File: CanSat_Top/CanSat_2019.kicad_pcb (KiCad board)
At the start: 6 copper layers, 65 x 65 mm, 152 parts, among them J10 20 Pin FFC, J3 Conn_SWD_10, J5 505110-1292 FFC, J6 0734120114, J7 Micro_SD_Card_Det_Hirose_DM3AT, J8 AVR-ISP-6, J9 20Pin FFC, Q1 SSM3J338R, Q2 SSM3J338R, Q3 SSM3J338R, SW1 SW_Push, SW2 SW_Push, SW3 SW_Push, SW4 SW_Push, U1 INA260, U10 W25M02GV, U11 M24M02-DRMN6TB, U12 BME280, U13 BME280, U14 BME280, U15 DS18B20U, U16 DS18B20U, U17 DS18B20U, U2 STM32H743ZITx, U21 ATTINY85-20SU, U3 TPS62132, U4 PA6H, U5 RFM69HCW, U6 APDS-9960, U7 CM1624, U8 BNO055, U9 MPU-9250, Y1 SIT1533AI-H4-DCC-32_768E

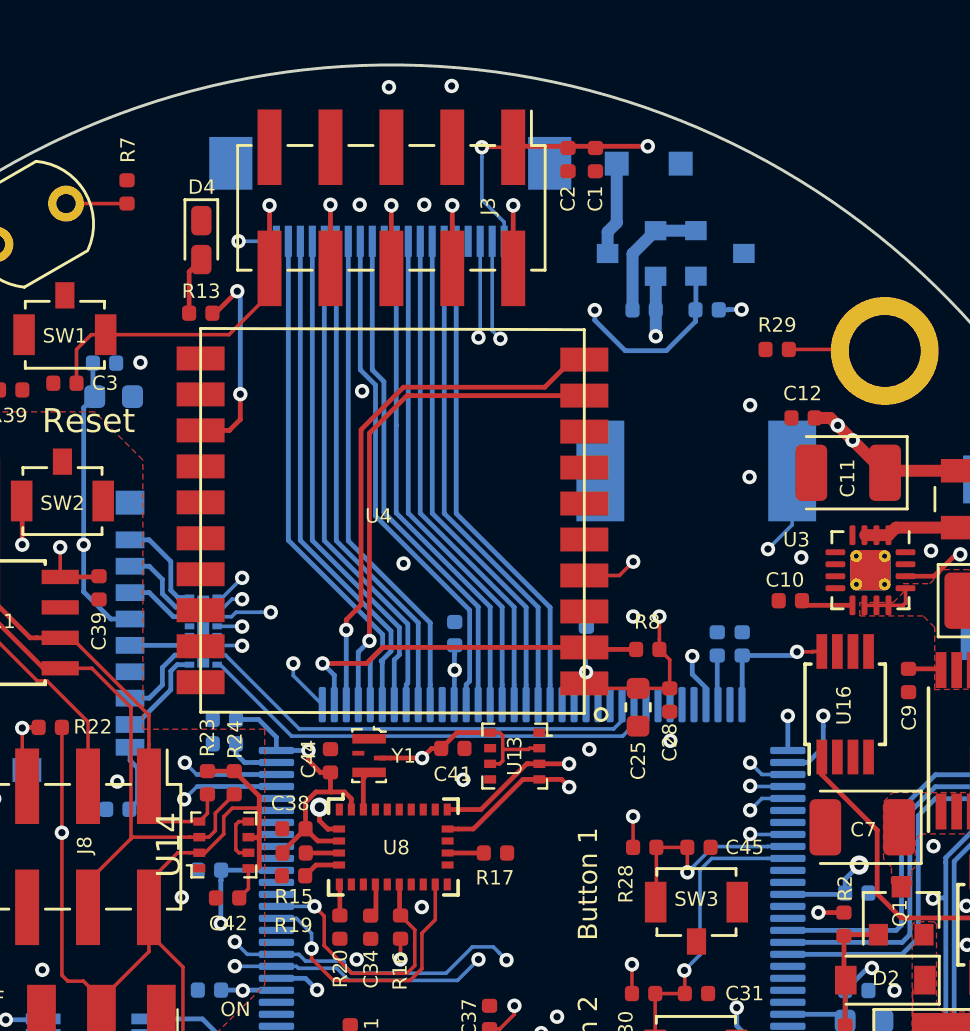
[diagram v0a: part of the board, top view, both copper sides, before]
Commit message: Added OneWire Header and finished bottom PCB design
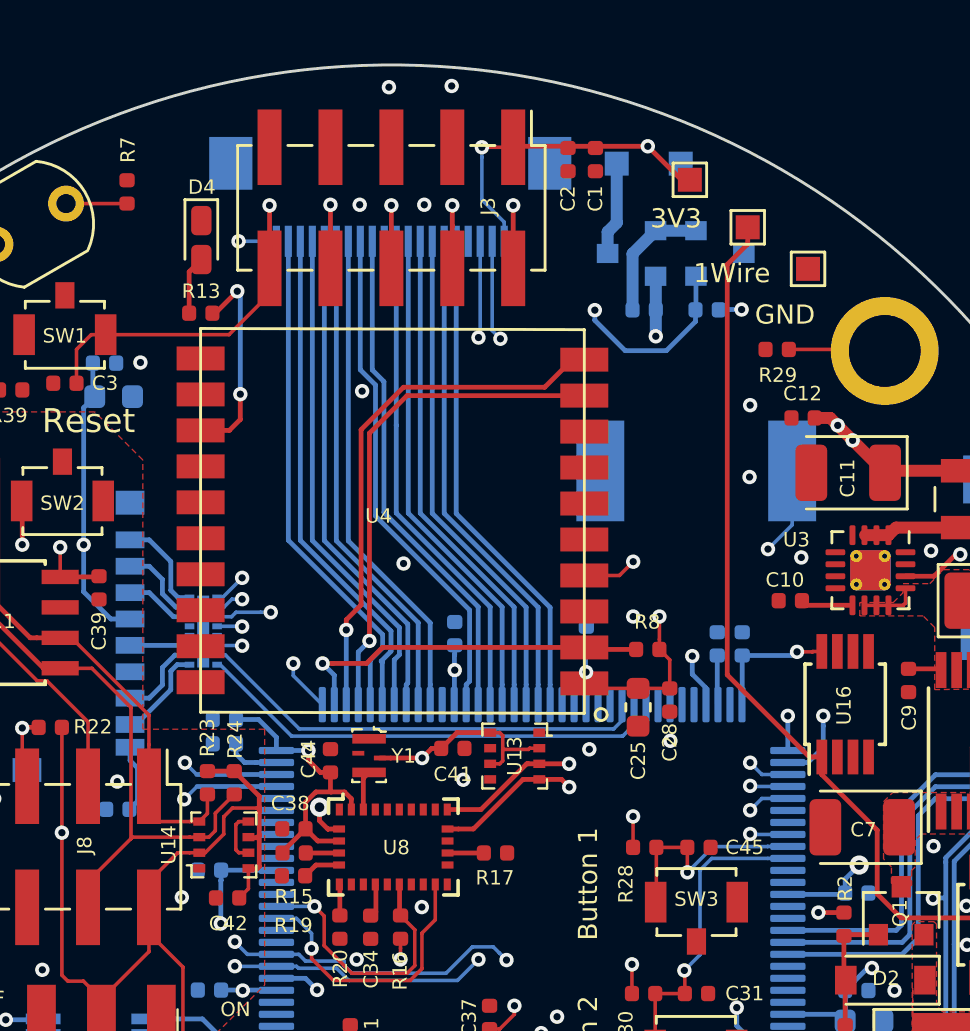
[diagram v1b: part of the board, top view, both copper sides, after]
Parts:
- added TP18: DS18B20 3V3, TestPoint:TestPoint_Pad_1.0x1.0mm, F.Cu at (84.8, 51.0)
- added TP19: OneWire, TestPoint:TestPoint_Pad_1.0x1.0mm, F.Cu at (87.2, 53.0)
- added TP20: DS18B20 GND, TestPoint:TestPoint_Pad_1.0x1.0mm, F.Cu at (89.8, 54.7)
- R28, R30: value 10k -> 1M
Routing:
- net /OneWire: track 55.8 -> 80.2 mm
- net +3V3: track 193.0 -> 195.3 mm
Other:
- board text added: "1Wire"
